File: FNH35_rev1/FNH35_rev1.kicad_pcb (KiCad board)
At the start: 2 copper layers, 126.2 x 116.7 mm, 232 parts, among them J1 Conn_01x03, J101 Conn_01x03, J102 DX07B024JJ3R1600, J103 Conn_01x08, J2 Conn_01x08, J3 DX07B024JJ3R1600, K0 KEYSW, K1 KEYSW, K10 KEYSW, K11 KEYSW, K12 KEYSW, K2 KEYSW, K20 KEYSW, K201 KEYSW, K202 KEYSW, K203 KEYSW, K204 KEYSW, K205 KEYSW, K206 KEYSW, K207 KEYSW, K208 KEYSW, K209 KEYSW, K21 KEYSW, K210 KEYSW, K211 KEYSW, K212 KEYSW, K213 KEYSW, K214 KEYSW, K215 KEYSW, K216 KEYSW, K217 KEYSW, K218 KEYSW, K22 KEYSW, K23 KEYSW, K30 KEYSW, K31 KEYSW, K32 KEYSW, K33 KEYSW, K40 KEYSW, K41 KEYSW, K42 KEYSW, K43 KEYSW, SW1 SW_PUSH, SW101 SW_PUSH, U1 STM32F303CCTx, U101 LD1117S33TR_SOT223, U102 STM32F303CCTx, U103 74AHCT125, U2 LD1117S33TR_SOT223, U3 74AHCT125, X1 XTAL_GND, X101 XTAL_GND

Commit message: finished, again
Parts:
- removed D1, D101: PRTR5V0U2X,215, tm-kicad-lib:PRTR5V0U2X,215
- added IC1: NUF2221W1T2G, NUF2221W1T2G:SOT-363, F.Cu at (-10.5, 34.5)
- added IC12: NUF2221W1T2G, NUF2221W1T2G:SOT-363, F.Cu at (43.1, 37.3)
- moved C112 55.6 mm to (-34.1, 93.0), turned to 270 degrees
- moved C107 40.4 mm to (-88.5, 96.6), turned to 225 degrees
- moved C110 39.5 mm to (-45.5, 103.0), turned to 135 degrees
- moved C108 38.5 mm to (-48.1, 105.5), turned to 135 degrees
- moved C109 38.4 mm to (-86.5, 108.6), turned to 315 degrees
- moved U101 37.5 mm to (-44.3, 96.7), turned to 135 degrees
- moved X101 32.1 mm to (-84.1, 101.7), turned to 270 degrees
- moved C111 28.2 mm to (-51.9, 97.9), turned to 135 degrees
- moved R102 15.9 mm to (-73.5, 108.2), turned to 45 degrees
- moved DS204 15.5 mm to (10.9, 119.0), turned to 270 degrees
- moved DS217 15.1 mm to (-91.1, 56.8), turned to 270 degrees
- moved DS208 14.9 mm to (-6.06, 111.0), turned to 270 degrees
- moved DS203 14.9 mm to (-15.1, 75.9), turned to 270 degrees
- moved DS212 14.3 mm to (-26.1, 108.0), turned to 270 degrees
- moved DS209 14.3 mm to (-53.7, 27.9), turned to 270 degrees
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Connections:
- DS201 pad 1: /row0 -> /Lrow0
- DS202 pad 1: /row1 -> /Lrow1
- DS203 pad 1: /row2 -> /Lrow2
- DS204 pad 1: /row3 -> /Lrow3
- DS205 pad 1: /row0 -> /Lrow0
- DS206 pad 1: /row1 -> /Lrow1
- DS207 pad 1: /row2 -> /Lrow2
- DS208 pad 1: /row3 -> /Lrow3
- DS209 pad 1: /row0 -> /Lrow0
- DS210 pad 1: /row1 -> /Lrow1
- DS211 pad 1: /row2 -> /Lrow2
- DS212 pad 1: /row3 -> /Lrow3
- DS213 pad 1: /row0 -> /Lrow0
- DS214 pad 1: /row1 -> /Lrow1
- DS215 pad 1: /row2 -> /Lrow2
- DS216 pad 1: /row0 -> /Lrow0
- DS217 pad 1: /row1 -> /Lrow1
- DS218 pad 1: /row2 -> /Lrow2
- J101 pad 3: /SerConn -> /LSerConn
- J102 pad A6: /DA+ -> /LDA+
- J102 pad A7: /DA- -> /LDA-
- J103 pad 3: /PA17 -> /LPA17
- J103 pad 4: /PA16 -> /LPA16
- J103 pad 5: /PA15 -> /LPA15
- J103 pad 6: /PA14 -> /LPA14
- J103 pad 7: /PA13 -> /LPA13
- K201 pad 1: /col4 -> /Lcol4
- K202 pad 1: /col4 -> /Lcol4
- K203 pad 1: /col4 -> /Lcol4
- K204 pad 1: /col4 -> /Lcol4
- K205 pad 1: /col3 -> /Lcol3
- K206 pad 1: /col3 -> /Lcol3
- K207 pad 1: /col3 -> /Lcol3
- K208 pad 1: /col3 -> /Lcol3
- K209 pad 1: /col2 -> /Lcol2
- K210 pad 1: /col2 -> /Lcol2
- K211 pad 1: /col2 -> /Lcol2
- K212 pad 1: /col2 -> /Lcol2
- K213 pad 1: /col1 -> /Lcol1
- K214 pad 1: /col1 -> /Lcol1
- K215 pad 1: /col1 -> /Lcol1
- K216 pad 1: /col0 -> /Lcol0
- K217 pad 1: /col0 -> /Lcol0
- K218 pad 1: /col0 -> /Lcol0
- R101 pad 1: /ADC -> /LADC
- R102 pad 2: /ADC -> /LADC
- R103 pad 1: /BOOT -> /LBOOT
- SW101 pad 2: /BOOT -> /LBOOT
- U1 pad 32: /DA- -> /USB-
- U1 pad 33: /DA+ -> /USB+
- U102 pad 10: /ADC -> /LADC
- U102 pad 13: /PA13 -> /LPA13
- U102 pad 14: /PA14 -> /LPA14
- U102 pad 15: /PA15 -> /LPA15
- U102 pad 16: /PA16 -> /LPA16
- U102 pad 17: /PA17 -> /LPA17
- U102 pad 19: /CKI_Back -> /LCKI_Back
- U102 pad 20: /SDI_Back -> /LSDI_Back
- U102 pad 21: /CKI_Und -> /LCKI_Und
- U102 pad 22: /SDI_Und -> /LSDI_Und
- U102 pad 26: /PB13 -> Net-(U102-Pad26)
- U102 pad 27: /PB14 -> Net-(U102-Pad27)
- U102 pad 28: /SerConn -> /LSerConn
- U102 pad 32: /DA- -> /LUSB-
- U102 pad 33: /DA+ -> /LUSB+
- U102 pad 37: /row3 -> /Lrow3
- U102 pad 38: /row2 -> /Lrow2
- U102 pad 39: /row1 -> /Lrow1
- U102 pad 40: /row0 -> /Lrow0
- U102 pad 41: /col4 -> /Lcol4
- U102 pad 42: /col3 -> /Lcol3
- U102 pad 43: /col2 -> /Lcol2
- U102 pad 44: /BOOT -> /LBOOT
- U102 pad 45: /col1 -> /Lcol1
- U102 pad 46: /col0 -> /Lcol0
- U103 pad 12: /CKI_Back -> /LCKI_Back
- U103 pad 2: /SDI_Und -> /LSDI_Und
- U103 pad 5: /CKI_Und -> /LCKI_Und
- U103 pad 9: /SDI_Back -> /LSDI_Back
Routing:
- net GND: track 1026.3 -> 2126.9 mm, vias 44 -> 104
- net +5V: track 1063.4 -> 2005.2 mm, vias 57 -> 111
- net /LSerConn: track 0.00 -> 188.0 mm, vias 0 -> 1
- net /Lrow0: track 0.00 -> 180.4 mm, vias 0 -> 7
- net /LCKI_Und: track 0.00 -> 147.0 mm, vias 0 -> 2
- net +3V3: track 168.5 -> 314.4 mm, vias 9 -> 14
- net /LSDI_Und: track 0.00 -> 143.2 mm, vias 0 -> 4
- net /Lcol2: track 0.00 -> 142.6 mm, vias 0 -> 8
- net Net-(DB311-Pad3): track 0.00 -> 142.5 mm, vias 0 -> 4
- net /Lcol4: track 0.00 -> 141.8 mm, vias 0 -> 10
- net /LCKI_Back: track 0.00 -> 141.3 mm, vias 0 -> 4
- net /DA+: track 151.7 -> 10.5 mm, vias 5 -> 1
- net /LSDI_Back: track 0.00 -> 140.1 mm, vias 0 -> 4
- net /Lrow1: track 0.00 -> 139.1 mm, vias 0 -> 5
- net /USB+: track 0.00 -> 138.4 mm, vias 0 -> 4
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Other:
- board size 126.2 x 116.7 mm -> 253.4 x 116.7 mm

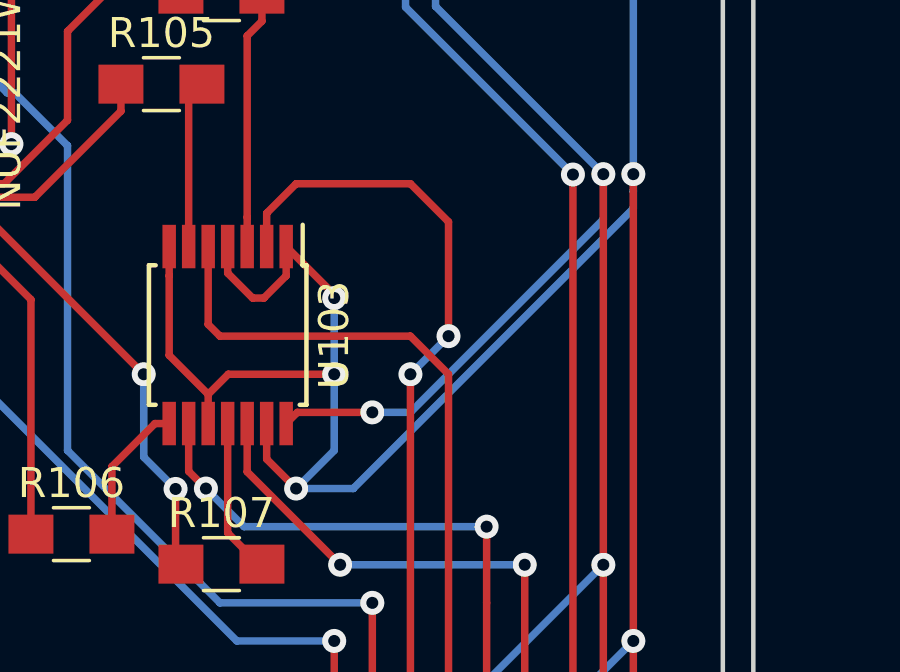
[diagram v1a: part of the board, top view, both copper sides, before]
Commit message: separated left half
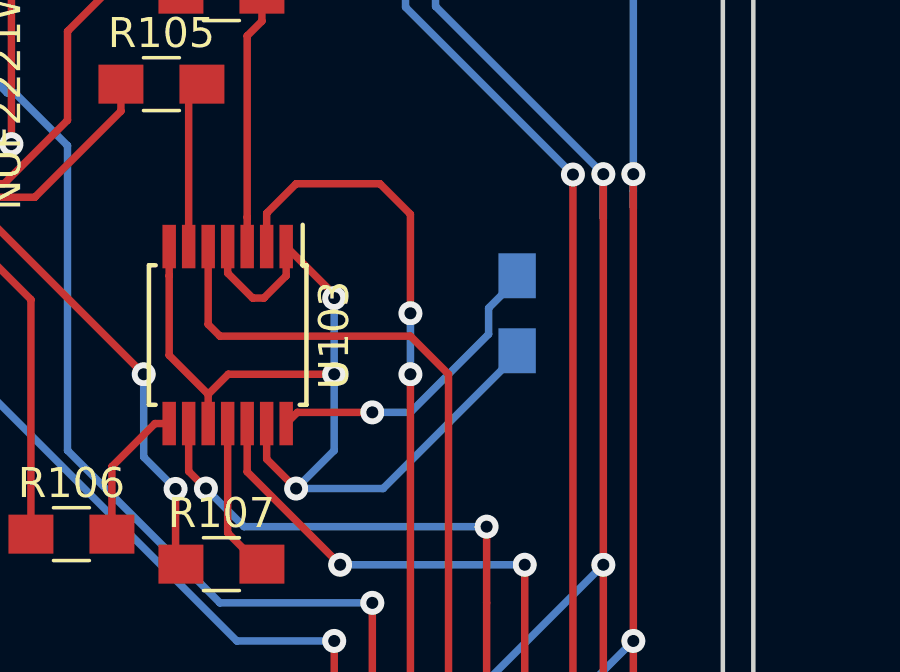
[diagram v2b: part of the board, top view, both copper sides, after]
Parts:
- added C113: 0.1u, Capacitors_SMD:C_0805_HandSoldering, B.Cu at (8.79, 43.7)
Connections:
- C101 pad 2: GND -> GNDA
- C102 pad 2: GND -> GNDA
- C103 pad 2: GND -> GNDA
- C104 pad 2: GND -> GNDA
- C105 pad 2: GND -> GNDA
- C106 pad 2: GND -> GNDA
- C107 pad 2: GND -> GNDA
- C108 pad 1: +5V -> +5VA
- C108 pad 2: GND -> GNDA
- C109 pad 2: GND -> GNDA
- C110 pad 1: +5V -> +5VA
- C110 pad 2: GND -> GNDA
- C111 pad 2: GND -> GNDA
- C112 pad 1: +5V -> +5VA
- C112 pad 2: GND -> GNDA
- CB301 pad 1: +5V -> +5VA
- CB301 pad 2: GND -> GNDA
- CB302 pad 1: +5V -> +5VA
- CB302 pad 2: GND -> GNDA
- CB303 pad 1: GND -> GNDA
- CB303 pad 2: +5V -> +5VA
- CB304 pad 1: GND -> GNDA
- CB304 pad 2: +5V -> +5VA
- CB305 pad 1: +5V -> +5VA
- CB305 pad 2: GND -> GNDA
- CB306 pad 1: +5V -> +5VA
- CB306 pad 2: GND -> GNDA
- CB307 pad 1: GND -> GNDA
- CB307 pad 2: +5V -> +5VA
- CB308 pad 1: GND -> GNDA
- CB308 pad 2: +5V -> +5VA
- CB309 pad 1: +5V -> +5VA
- CB309 pad 2: GND -> GNDA
- CB310 pad 1: +5V -> +5VA
- CB310 pad 2: GND -> GNDA
- CB311 pad 1: GND -> GNDA
- CB311 pad 2: +5V -> +5VA
- CB312 pad 1: GND -> GNDA
- CB312 pad 2: +5V -> +5VA
- CB313 pad 1: +5V -> +5VA
- CB313 pad 2: GND -> GNDA
- CB314 pad 1: +5V -> +5VA
- CB314 pad 2: GND -> GNDA
- CB315 pad 1: GND -> GNDA
- CB315 pad 2: +5V -> +5VA
- CB316 pad 1: +5V -> +5VA
- CB316 pad 2: GND -> GNDA
- CB317 pad 1: +5V -> +5VA
- CB317 pad 2: GND -> GNDA
- CB318 pad 1: GND -> GNDA
- CB318 pad 2: +5V -> +5VA
- CU401 pad 1: +5V -> +5VA
- CU401 pad 2: GND -> GNDA
- CU402 pad 1: +5V -> +5VA
- CU402 pad 2: GND -> GNDA
- CU403 pad 1: GND -> GNDA
- CU403 pad 2: +5V -> +5VA
- CU404 pad 1: +5V -> +5VA
- CU404 pad 2: GND -> GNDA
- CU405 pad 1: GND -> GNDA
- CU405 pad 2: +5V -> +5VA
- CU406 pad 1: +5V -> +5VA
- CU406 pad 2: GND -> GNDA
- CU407 pad 1: GND -> GNDA
- CU407 pad 2: +5V -> +5VA
- CU408 pad 1: GND -> GNDA
- CU408 pad 2: +5V -> +5VA
- DB301 pad 4: GND -> GNDA
- DB301 pad 5: +5V -> +5VA
- DB302 pad 4: GND -> GNDA
- DB302 pad 5: +5V -> +5VA
- DB303 pad 1: /LEDMatrix_perKey/SDO -> /LKSDO
- DB303 pad 4: GND -> GNDA
- DB303 pad 5: +5V -> +5VA
- DB303 pad 6: /LEDMatrix_perKey/CKO -> /LKCKO
- DB304 pad 4: GND -> GNDA
- DB304 pad 5: +5V -> +5VA
- DB305 pad 4: GND -> GNDA
- DB305 pad 5: +5V -> +5VA
- DB306 pad 4: GND -> GNDA
- DB306 pad 5: +5V -> +5VA
- DB307 pad 4: GND -> GNDA
- DB307 pad 5: +5V -> +5VA
- DB308 pad 4: GND -> GNDA
- DB308 pad 5: +5V -> +5VA
- DB309 pad 4: GND -> GNDA
- DB309 pad 5: +5V -> +5VA
- DB310 pad 4: GND -> GNDA
- DB310 pad 5: +5V -> +5VA
- DB311 pad 4: GND -> GNDA
- DB311 pad 5: +5V -> +5VA
- DB312 pad 4: GND -> GNDA
- DB312 pad 5: +5V -> +5VA
- DB313 pad 4: GND -> GNDA
- DB313 pad 5: +5V -> +5VA
- DB314 pad 4: GND -> GNDA
- DB314 pad 5: +5V -> +5VA
- DB315 pad 4: GND -> GNDA
- DB315 pad 5: +5V -> +5VA
- DB316 pad 4: GND -> GNDA
- DB316 pad 5: +5V -> +5VA
- DB317 pad 4: GND -> GNDA
- DB317 pad 5: +5V -> +5VA
- DB318 pad 4: GND -> GNDA
- DB318 pad 5: +5V -> +5VA
- DR401 pad 1: /LEDMatrix_Underglow/SDO -> /LUSDO
- DR401 pad 4: GND -> GNDA
- DR401 pad 5: +5V -> +5VA
- DR401 pad 6: /LEDMatrix_Underglow/CKO -> /LUCKO
- DR402 pad 4: GND -> GNDA
- DR402 pad 5: +5V -> +5VA
- DR403 pad 4: GND -> GNDA
- DR403 pad 5: +5V -> +5VA
- DR404 pad 4: GND -> GNDA
- DR404 pad 5: +5V -> +5VA
- DR405 pad 4: GND -> GNDA
- DR405 pad 5: +5V -> +5VA
- DR406 pad 4: GND -> GNDA
- DR406 pad 5: +5V -> +5VA
- DR407 pad 4: GND -> GNDA
- DR407 pad 5: +5V -> +5VA
- DR408 pad 4: GND -> GNDA
- DR408 pad 5: +5V -> +5VA
- IC1 pad 2: GND -> GNDA
- IC1 pad 5: +5V -> +5VA
- J101 pad 1: GND -> GNDA
- J102 pad A1: GND -> GNDA
- J102 pad A12: GND -> GNDA
- J102 pad A4: +5V -> +5VA
- J102 pad A9: +5V -> +5VA
- J102 pad B1: GND -> GNDA
- J102 pad B12: GND -> GNDA
- J102 pad B4: +5V -> +5VA
- J102 pad B9: +5V -> +5VA
- J102 pad S1: GND -> GNDA
- J102 pad S2: GND -> GNDA
- J102 pad S3: GND -> GNDA
- J102 pad S4: GND -> GNDA
- J102 pad S5: GND -> GNDA
- J102 pad S6: GND -> GNDA
- J103 pad 1: GND -> GNDA
- J103 pad 2: +5V -> +5VA
- R101 pad 2: +5V -> +5VA
- R102 pad 1: GND -> GNDA
- R103 pad 2: GND -> GNDA
- U101 pad 1: GND -> GNDA
- U101 pad 3: +5V -> +5VA
- U102 pad 23: GND -> GNDA
- U102 pad 35: GND -> GNDA
- U102 pad 47: GND -> GNDA
- U102 pad 8: GND -> GNDA
- U103 pad 1: GND -> GNDA
- U103 pad 10: GND -> GNDA
- U103 pad 13: GND -> GNDA
- U103 pad 14: +5V -> +5VA
- U103 pad 4: GND -> GNDA
- U103 pad 7: GND -> GNDA
- X101 pad 3: GND -> GNDA
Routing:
- net GND: track 2126.9 -> 1064.9 mm, vias 104 -> 48
- net GNDA: track 0.00 -> 1056.3 mm, vias 0 -> 56
- net +5V: track 2005.2 -> 1991.8 mm, vias 111 -> 110
- net +5VA: track 0.00 -> 10.3 mm, vias 0 -> 1
- net /LSDI_Und: track 143.2 -> 141.6 mm

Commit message: start of case design
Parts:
- removed C1, C107, C109, C2: 33pf, Capacitors_SMD:C_0805_HandSoldering
- removed C10, C108, C111, C112, C4, C9: 10u, Capacitors_SMD:C_0805_HandSoldering
- removed C101, C11: 4.7u, Capacitors_SMD:C_0805_HandSoldering
- removed C102, C103, C104, C105, C113, C5, C6, C7, C8, CB0, CB1, CB10, CB11, CB12, CB2, CB20, CB21, CB22, CB23, CB30, CB301, CB302, CB303, CB304, CB305, CB306, CB307, CB308, CB309, CB31, CB310, CB311, CB312, CB313, CB314, CB315, CB316, CB317, CB318, CB32, CB33, CB40, CB41, CB42, CB43, CU1, CU2, CU3, CU4, CU401, CU402, CU403, CU404, CU405, CU406, CU407, CU408, CU5, CU6, CU7, CU8: 0.1u, Capacitors_SMD:C_0805_HandSoldering
- removed C106, C12: 1u, Capacitors_SMD:C_0805_HandSoldering
- removed C110, C3: 100n, Capacitors_SMD:C_0805_HandSoldering
- removed DB0, DB1, DB10, DB11, DB12, DB2, DB20, DB21, DB22, DB23, DB30, DB301, DB302, DB303, DB304, DB305, DB306, DB307, DB308, DB309, DB31, DB310, DB311, DB312, DB313, DB314, DB315, DB316, DB317, DB318, DB32, DB33, DB40, DB41, DB42, DB43, DR401, DR402, DR403, DR404, DR405, DR406, DR407, DR408, DU1, DU2, DU3, DU4, DU5, DU6, DU7, DU8: APA102, gsg-modules:APA102-2020
- removed DS0, DS1, DS10, DS11, DS12, DS2, DS20, DS201, DS202, DS203, DS204, DS205, DS206, DS207, DS208, DS209, DS21, DS210, DS211, DS212, DS213, DS214, DS215, DS216, DS217, DS218, DS22, DS23, DS30, DS31, DS32, DS33, DS40, DS41, DS42, DS43: D, keyboard_parts:D_SOD123_hand
- removed IC1, IC12: NUF2221W1T2G, NUF2221W1T2G:SOT-363
- removed J1, J101: Conn_01x03, Connectors_JST:JST_SH_BM03B-SRSS-TB_03x1.00mm_Straight
- removed J102, J3: DX07B024JJ3R1600, butts:JAE_DX07B024JJ3R1600
- removed J103, J2: Conn_01x08, Pin_Headers:Pin_Header_Angled_1x08_Pitch1.27mm
- removed K0, K1, K10, K11, K12, K2, K20, K201, K202, K203, K204, K205, K206, K207, K208, K209, K21, K210, K211, K212, K213, K214, K215, K216, K217, K218, K22, K23, K30, K31, K32, K33, K40, K41, K42, K43: KEYSW, keyswitches:Kailh_socket
- removed R1, R104, R105, R106, R107, R2, R3, R4: 300, Resistors_SMD:R_0805_HandSoldering
- removed R101, R6: 4k1, Resistors_SMD:R_0805_HandSoldering
- removed R102, R7: 9k1, Resistors_SMD:R_0805_HandSoldering
- removed R103, R5: 10kR, Resistors_SMD:R_0805_HandSoldering
- removed SW1, SW101: SW_PUSH, Buttons_Switches_SMD:SW_SPST_TL3342
- removed U1, U102: STM32F303CCTx, QFP50P900X900X160-48N:QFP50P900X900X160-48N
- removed U101, U2: LD1117S33TR_SOT223, TO_SOT_Packages_SMD:SOT-223-3_TabPin2
- removed U103, U3: 74AHCT125, Housings_SSOP:TSSOP-14_4.4x5mm_Pitch0.65mm
- removed X1, X101: XTAL_GND, Crystals:Crystal_SMD_0603-4pin_6.0x3.5mm_HandSoldering
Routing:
- net +5V: track 1991.8 -> 0.00 mm, vias 110 -> 0
- net GND: track 1064.9 -> 0.00 mm, vias 48 -> 0
- net GNDA: track 1056.3 -> 0.00 mm, vias 56 -> 0
- net +3V3: track 314.4 -> 0.00 mm, vias 14 -> 0
- net /SerConn: track 257.9 -> 0.00 mm, vias 1 -> 0
- net /row0: track 193.1 -> 0.00 mm, vias 12 -> 0
- net /LSerConn: track 188.0 -> 0.00 mm, vias 1 -> 0
- net /Lrow0: track 180.4 -> 0.00 mm, vias 7 -> 0
- net /row1: track 175.7 -> 0.00 mm, vias 5 -> 0
- net /row2: track 168.2 -> 0.00 mm, vias 9 -> 0
- net /col4: track 165.2 -> 0.00 mm, vias 5 -> 0
- net /col3: track 160.6 -> 0.00 mm, vias 10 -> 0
- net /SDI_Und: track 156.2 -> 0.00 mm, vias 6 -> 0
- net /CKI_Und: track 155.4 -> 0.00 mm, vias 4 -> 0
- net /SDI_Back: track 150.5 -> 0.00 mm, vias 6 -> 0
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- removed copper zone on B.Cu, net GND
- removed copper zone on F.Cu, net GND
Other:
- board outline removed
